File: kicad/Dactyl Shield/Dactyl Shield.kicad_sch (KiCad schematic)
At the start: 10 parts

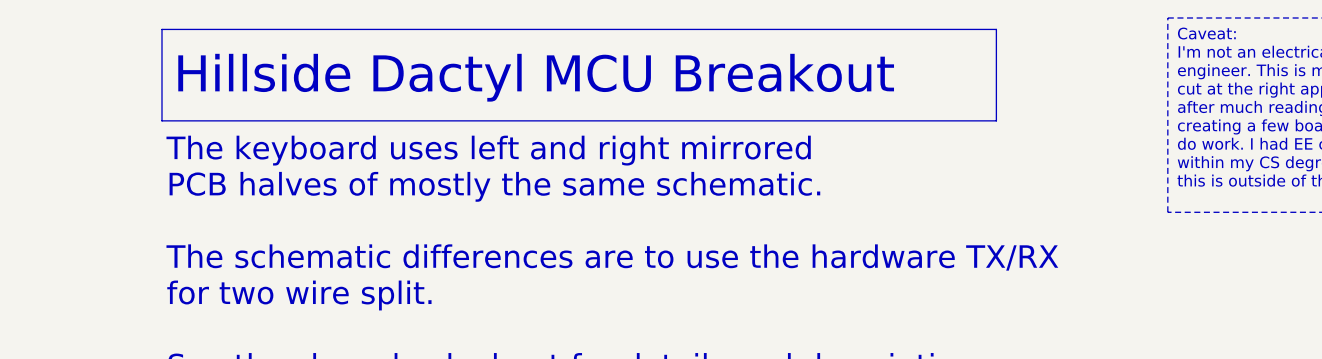
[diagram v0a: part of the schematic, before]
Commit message: reorg: update silks for new board name
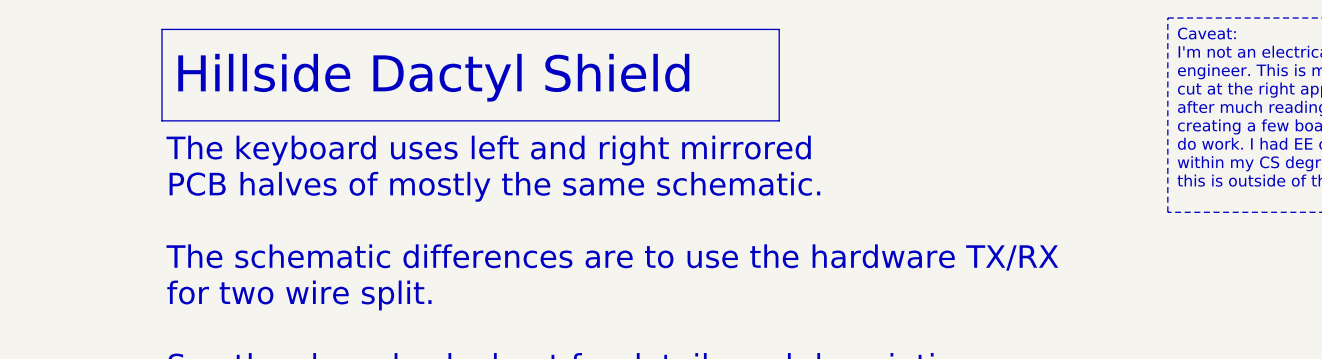
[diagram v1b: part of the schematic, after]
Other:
- title: Hillside Dactyl MCU Breakout -> Hillside Dactyl Shield
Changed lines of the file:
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@@
 	(paper "USLetter")
 	(title_block
-		(title "Hillside Dactyl MCU Breakout")
+		(title "Hillside Dactyl Shield")
 		(date "2024-06-04")
 		(rev "0.1.0-alpha.2")
@@
 		(comment 2 "  On board: reset, battery switch and LEDs")
 		(comment 3 "Provides:")
-		(comment 4 "MCU breakout for Dactyl split keyboards ")
+		(comment 4 "Shield for Dactyl split keyboards ")
 	)
 	(junction
@@
 	(polyline
 		(pts
-			(xy 90.17 57.15) (xy 182.88 57.15)
+			(xy 90.17 57.15) (xy 158.75 57.15)
 		)
 		(stroke
@@
 	(polyline
 		(pts
-			(xy 182.88 67.31) (xy 90.17 67.31)
+			(xy 158.75 67.31) (xy 90.17 67.31)
 		)
 		(stroke
@@
 	(polyline
 		(pts
-			(xy 182.88 57.15) (xy 182.88 67.31)
+			(xy 158.75 57.15) (xy 158.75 67.31)
 		)
 		(stroke
@@
 		)
 		(instances
-			(project "Dactyl MCU Breakout"
+			(project "Dactyl Shield"
 				(path "/454146f1-d25e-490f-a0db-4f993607d919"
 					(page "3")
@@
 		)
 		(instances
-			(project "Dactyl MCU Breakout"
+			(project "Dactyl Shield"
 				(path "/454146f1-d25e-490f-a0db-4f993607d919"
 					(page "2")
